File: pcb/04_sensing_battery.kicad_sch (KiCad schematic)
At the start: 0 parts

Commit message: Added VBAT sensing via a voltage divider to stay within the MCU 3V3 limit
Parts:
- added C401: 100n 50V, FluxNode-FOC:C_0402_1005_DensityHigh, symbol Device:C
- added R401: 100k 1%, FluxNode-FOC:R_0402_1005_DensityHigh, symbol Device:R
- added R402: 8k2 1%, FluxNode-FOC:R_0402_1005_DensityHigh, symbol Device:R
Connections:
- new net GND: C401.2, R402.2
- new net SENSE_VBAT: C401.1, R401.2, R402.1
- new net VIN: R401.1

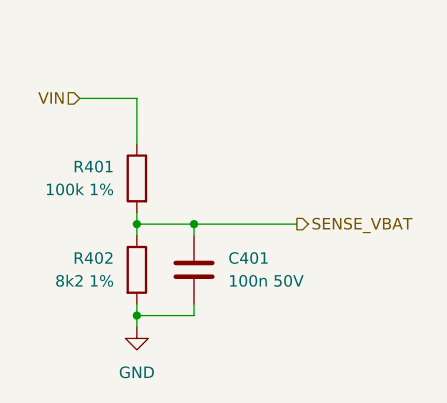
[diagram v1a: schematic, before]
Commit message: Unified all different LCSC part numbers of the same exact components to just one variant
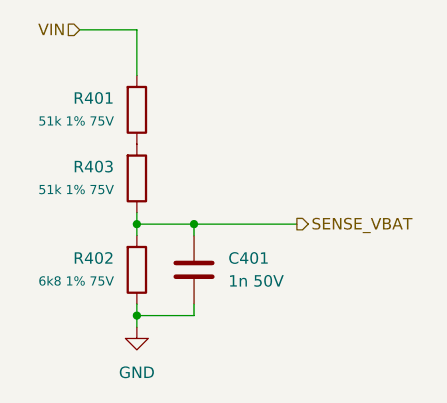
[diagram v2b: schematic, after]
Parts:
- added R403: 51k 1% 75V, FluxNode-FOC:R_0603_1608_DensityHigh, symbol Device:R
- C401: value 100n 50V -> 1n 50V; LCSC (none) -> C466233; MPN (none) -> TCC0402X7R102K500AT
- R401: value 100k 1% -> 51k 1% 75V; footprint FluxNode-FOC:R_0402_1005_DensityHigh -> FluxNode-FOC:R_0603_1608_DensityHigh; LCSC (none) -> C2907049; MPN (none) -> FRC0603F5102TS
- R402: value 8k2 1% -> 6k8 1% 75V; footprint FluxNode-FOC:R_0402_1005_DensityHigh -> FluxNode-FOC:R_0603_1608_DensityHigh; LCSC (none) -> C2907055; MPN (none) -> FRC0603F6801TS
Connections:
- net GND: now also R402.1; no longer R402.2
- net SENSE_VBAT: now also R402.2, R403.1; no longer R401.2, R402.1
- net VIN: now also R401.2; no longer R401.1
- new net: R401.1, R403.2
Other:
- company: (none) -> PhiMai
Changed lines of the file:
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@@
 	(generator_version "10.0")
 	(paper "A4")
+	(title_block
+		(date "2026-06-07")
+		(rev "0.1.0")
+		(company "PhiMai")
+	)
 	(junction
 		(at 124.46 93.98)
@@
 	(wire
 		(pts
-			(xy 118.11 80.01) (xy 118.11 85.09)
-		)
-		(stroke
-			(width 0)
-			(type default)
-		)
-	)
-	(wire
-		(pts
-			(xy 111.76 80.01) (xy 118.11 80.01)
+			(xy 118.11 72.39) (xy 118.11 77.47)
+		)
+		(stroke
+			(width 0)
+			(type default)
+		)
+	)
+	(wire
+		(pts
+			(xy 111.76 72.39) (xy 118.11 72.39)
 		)
 		(stroke
@@
 	(hierarchical_label "VIN"
 		(shape input)
-		(at 111.76 80.01 180)
+		(at 111.76 72.39 180)
 		(effects
 			(font
@@
 		(lib_id "Device:R")
 		(at 118.11 99.06 0)
+		(mirror x)
 		(unit 1)
 		(body_style 1)
@@
 			)
 		)
-		(property "Value" "8k2 1%"
+		(property "Value" "6k8 1% 75V"
 			(at 115.57 100.3299 0)
 			(show_name no)
@@
 			(effects
 				(font
-					(size 1.27 1.27)
+					(size 1.016 1.016)
 				)
 				(justify right)
 			)
 		)
-		(property "Footprint" "FluxNode-FOC:R_0402_1005_DensityHigh"
+		(property "Footprint" "FluxNode-FOC:R_0603_1608_DensityHigh"
 			(at 116.332 99.06 90)
 			(hide yes)
@@
 			)
 		)
-		(property "Description" "Resistor"
+		(property "Description" "RES 6.8kΩ ±1% 100mW 0603"
 			(at 118.11 99.06 0)
+			(hide yes)
+			(show_name no)
+			(do_not_autoplace no)
+			(effects
+				(font
+					(size 1.27 1.27)
+				)
+			)
+		)
+		(property "MPN" "FRC0603F6801TS"
+			(at 118.11 99.06 90)
+			(hide yes)
+			(show_name no)
+			(do_not_autoplace no)
+			(effects
+				(font
+					(size 1.27 1.27)
+				)
+			)
+		)
+		(property "LCSC" "C2907055"
+			(at 118.11 99.06 90)
 			(hide yes)
 			(show_name no)
@@
 			)
 		)
-		(property "Value" "100n 50V"
+		(property "Value" "1n 50V"
 			(at 128.27 100.3299 0)
 			(show_name no)
@@
 			)
 		)
-		(property "Description" "Unpolarized capacitor"
+		(property "Description" "CAP CER 1nF 50V X7R 0402"
+			(at 124.46 99.06 0)
+			(hide yes)
+			(show_name no)
+			(do_not_autoplace no)
+			(effects
+				(font
+					(size 1.27 1.27)
+				)
+			)
+		)
+		(property "MPN" "TCC0402X7R102K500AT"
+			(at 124.46 99.06 0)
+			(hide yes)
+			(show_name no)
+			(do_not_autoplace no)
+			(effects
+				(font
+					(size 1.27 1.27)
+				)
+			)
+		)
+		(property "LCSC" "C466233"
 			(at 124.46 99.06 0)
 			(hide yes)
@@
 	(symbol
 		(lib_id "Device:R")
-		(at 118.11 88.9 0)
-		(mirror y)
+		(at 118.11 81.28 0)
+		(mirror x)
 		(unit 1)
 		(body_style 1)
@@
 		(in_pos_files yes)
 		(dnp no)
-		(fields_autoplaced yes)
 		(property "Reference" "R401"
-			(at 115.57 87.6299 0)
-			(show_name no)
-			(do_not_autoplace no)
-			(effects
-				(font
-					(size 1.27 1.27)
-				)
-				(justify left)
-			)
-		)
-		(property "Value" "100k 1%"
-			(at 115.57 90.1699 0)
-			(show_name no)
-			(do_not_autoplace no)
-			(effects
-				(font
-					(size 1.27 1.27)
-				)
-				(justify left)
-			)
-		)
-		(property "Footprint" "FluxNode-FOC:R_0402_1005_DensityHigh"
-			(at 119.888 88.9 90)
+			(at 115.57 80.0099 0)
+			(show_name no)
+			(do_not_autoplace no)
+			(effects
+				(font
+					(size 1.27 1.27)
+				)
+				(justify right)
+			)
+		)
+		(property "Value" "51k 1% 75V"
+			(at 115.57 82.5499 0)
+			(show_name no)
+			(do_not_autoplace no)
+			(effects
+				(font
+					(size 1.016 1.016)
+				)
+				(justify right)
+			)
+		)
+		(property "Footprint" "FluxNode-FOC:R_0603_1608_DensityHigh"
+			(at 116.332 81.28 90)
 			(hide yes)
 			(show_name no)
@@
 		)
 		(property "Datasheet" ""
-			(at 118.11 88.9 0)
-			(hide yes)
-			(show_name no)
-			(do_not_autoplace no)
-			(effects
-				(font
-					(size 1.27 1.27)
-				)
-			)
-		)
-		(property "Description" "Resistor"
-			(at 118.11 88.9 0)
+			(at 118.11 81.28 0)
+			(hide yes)
+			(show_name no)
+			(do_not_autoplace no)
+			(effects
+				(font
+					(size 1.27 1.27)
+				)
+			)
+		)
+		(property "Description" "RES 51kΩ ±1% 100mW 0603"
+			(at 118.11 81.28 0)
+			(hide yes)
+			(show_name no)
+			(do_not_autoplace no)
+			(effects
+				(font
+					(size 1.27 1.27)
+				)
+			)
+		)
+		(property "MPN" "FRC0603F5102TS"
+			(at 118.11 81.28 90)
+			(hide yes)
+			(show_name no)
+			(do_not_autoplace no)
+			(effects
+				(font
+					(size 1.27 1.27)
+				)
+			)
+		)
+		(property "LCSC" "C2907049"
+			(at 118.11 81.28 90)
 			(hide yes)
 			(show_name no)
@@
 					(unit 1)
 				)
+			)
+		)
+	)
+	(symbol
+		(lib_id "Device:R")
+		(at 118.11 88.9 0)
+		(mirror x)
+		(unit 1)
+		(body_style 1)
+		(exclude_from_sim no)
+		(in_bom yes)
+		(on_board yes)
+		(in_pos_files yes)
+		(dnp no)
+		(property "Reference" "R403"
+			(at 115.57 87.6299 0)
+			(show_name no)
+			(do_not_autoplace no)
+			(effects
+				(font
+					(size 1.27 1.27)
+				)
+				(justify right)
+			)
+		)
+		(property "Value" "51k 1% 75V"
+			(at 115.57 90.1699 0)
+			(show_name no)
+			(do_not_autoplace no)
+			(effects
+				(font
+					(size 1.016 1.016)
+				)
+				(justify right)
+			)
+		)
+		(property "Footprint" "FluxNode-FOC:R_0603_1608_DensityHigh"
+			(at 116.332 88.9 90)
+			(hide yes)
+			(show_name no)
+			(do_not_autoplace no)
+			(effects
+				(font
+					(size 1.27 1.27)
+				)
+			)
+		)
+		(property "Datasheet" ""
+			(at 118.11 88.9 0)
+			(hide yes)
+			(show_name no)
+			(do_not_autoplace no)
+			(effects
+				(font
+					(size 1.27 1.27)
+				)
+			)
+		)
+		(property "Description" "RES 51kΩ ±1% 100mW 0603"
+			(at 118.11 88.9 0)
+			(hide yes)
+			(show_name no)
+			(do_not_autoplace no)
+			(effects
+				(font
+					(size 1.27 1.27)
+				)
+			)
+		)
+		(property "MPN" "FRC0603F5102TS"
+			(at 118.11 88.9 90)
+			(hide yes)
+			(show_name no)
+			(do_not_autoplace no)
+			(effects
+				(font
+					(size 1.27 1.27)
+				)
+			)
+		)
+		(property "LCSC" "C2907049"
+			(at 118.11 88.9 90)
+			(hide yes)
+			(show_name no)
+			(do_not_autoplace no)
+			(effects
+				(font
+					(size 1.27 1.27)
+				)
+			)
+		)
+		(pin "1"
+		)
+		(pin "2"
+		)
+		(instances
+			(project "FluxNode-FOC"
+				(path "/c3755418-04f3-4b36-86ed-bd05a53b8f5f/4a7f80da-7784-4b13-96a5-3c0ed1c95465"
+					(reference "R403")
+					(unit 1)
+				)
